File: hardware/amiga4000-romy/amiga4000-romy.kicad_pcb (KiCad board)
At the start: 2 copper layers, 37.3 x 37.9 mm, 6 parts

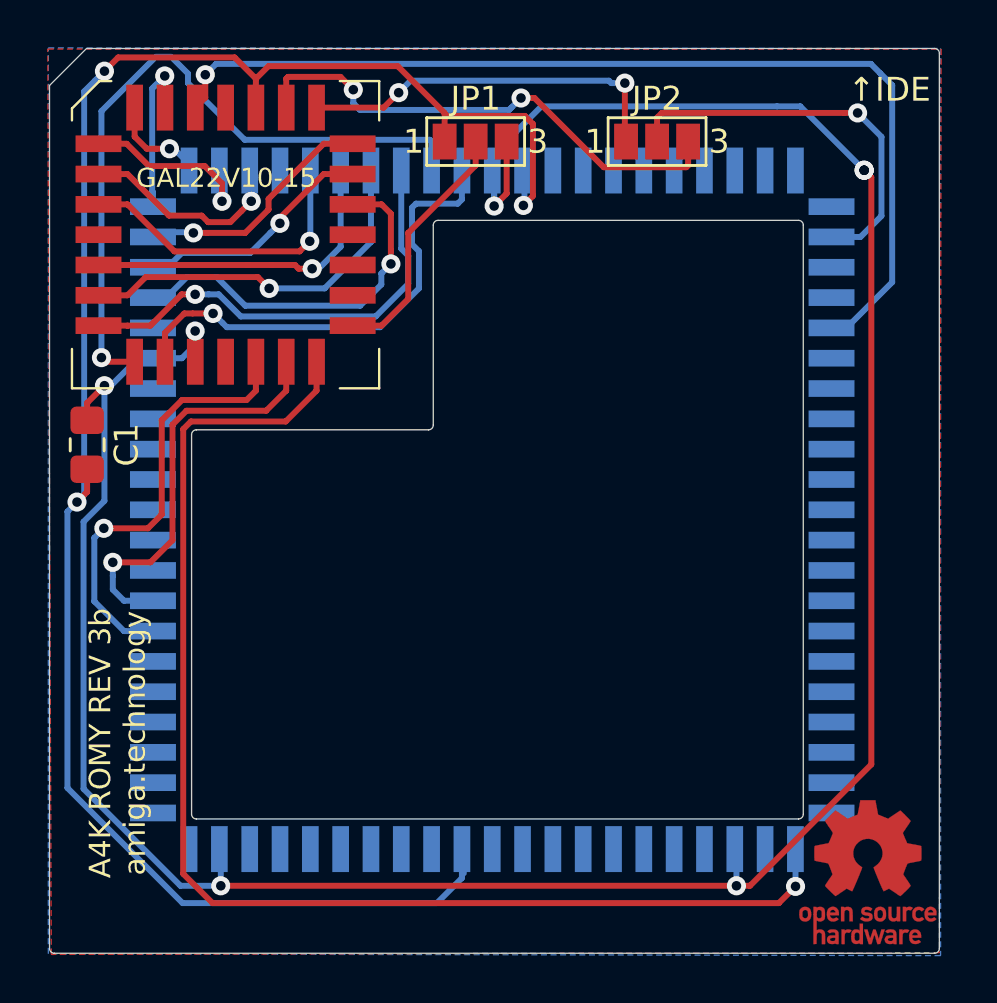
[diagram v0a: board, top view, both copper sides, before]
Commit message: Minor update to A4000 ROMY
- rounder edges
- slightly better routing
- preset jumpers for two less solder joints
- move to KiCAD 6.0rc
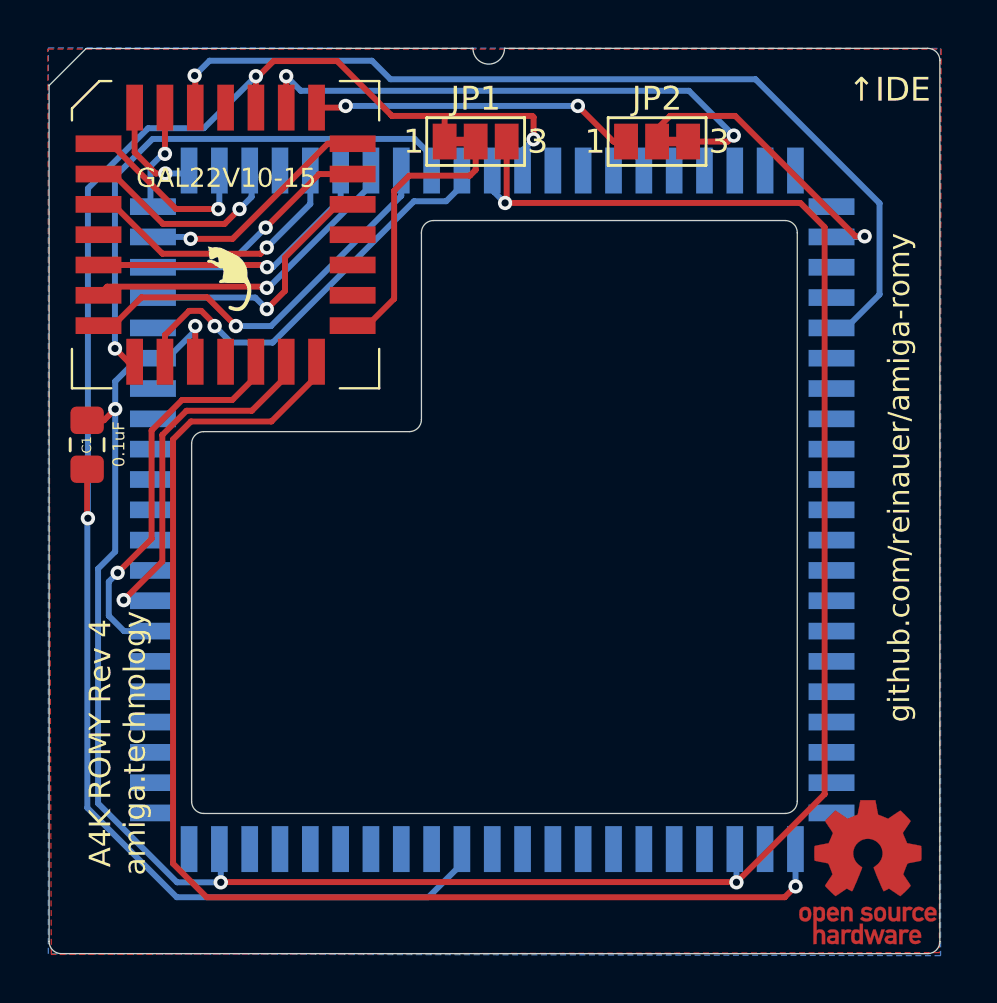
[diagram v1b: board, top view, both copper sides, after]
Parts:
- JP1: footprint Jumper:SolderJumper-3_P1.3mm_Open_Pad1.0x1.5mm_NumberLabels -> Amiga:SolderJumper-3_P1.3mm_Closed_12_Pad1.0x1.5mm_NumberLabels
- JP2: footprint Jumper:SolderJumper-3_P1.3mm_Open_Pad1.0x1.5mm_NumberLabels -> Amiga:SolderJumper-3_P1.3mm_Closed_23_Pad1.0x1.5mm_NumberLabels
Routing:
- net Net-(C1-Pad1): track 116.8 -> 104.3 mm, vias 7 -> 5
- net Net-(C1-Pad2): track 81.0 -> 73.0 mm
- net Net-(IC1-Pad12): track 30.7 -> 24.3 mm
- net Net-(IC1-Pad23): track 16.9 -> 12.4 mm
- net Net-(IC2-Pad73): track 16.7 -> 12.6 mm
- net Net-(IC1-Pad2): track 42.5 -> 39.2 mm
- net Net-(IC1-Pad3): track 7.04 -> 4.51 mm
- net Net-(IC1-Pad11): track 19.9 -> 17.6 mm
- net Net-(IC1-Pad26): track 15.9 -> 13.6 mm
- net Net-(IC1-Pad13): track 20.3 -> 18.1 mm
- net Net-(IC1-Pad16): track 18.5 -> 16.5 mm
- net Net-(IC1-Pad10): track 17.1 -> 15.3 mm
- net Net-(IC1-Pad17): track 17.3 -> 15.6 mm
- net Net-(IC1-Pad27): track 21.4 -> 23.0 mm
- net Net-(IC1-Pad9): track 13.8 -> 12.6 mm
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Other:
- outline, holes or cut-outs redrawn
- net class Default removed
- board text added: "A4K ROMY Rev 4 amiga.technology"
- board text added: "github.com/reinauer/amiga-romy"
- board text removed: "A4K ROMY REV 3b amiga.technology"
